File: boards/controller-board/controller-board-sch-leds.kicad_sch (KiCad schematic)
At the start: 60 parts, among them U10 MP2410A, U11 MP2410A, U6 MP2410A, U7 MP2410A, U8 MP2410A, U9 MP2410A

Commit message: Added LED test points. Added heatsinks and notes on thermal paste. Cleaned up bottom traces with new LED test points. Some hierarchical labels, some cleanup of schematic and layout. Builds.
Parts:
- added HS1, HS10, HS11, HS12, HS13, HS14, HS15, HS16, HS17, HS18, HS2, HS3, HS4, HS5, HS6, HS7, HS8, HS9: Heatsink, symbol Mechanical:Heatsink
- added TP25, TP26, TP27, TP28, TP29, TP30, TP31, TP32, TP33, TP34, TP35, TP36, TP37, TP38, TP39, TP4, TP40, TP41, TP42, TP43, TP5, TP6, TP7, TP8: TestPoint_Square, TestPoint:TestPoint_Pad_1.0x1.0mm, symbol Connector:TestPoint_Square
- C11, C13, C14, C20, C21, C22, C24, C27, C28, C30, C31, C33: DPN 1276-6767-1-ND -> 490-12456-1-ND; MFR Samsung Electro-Mechanics -> Murata Electronics; MPN CL31B106KBHNNNE -> GRT31CR61H106KE01L
- C12, C23, C25, C26, C29, C32: DPN 478-KGM15AR71H103KTCT-ND -> 399-12983-1-ND; MFR KYOCERA AVX -> KEMET; MPN KGM15AR71H103KT -> C0603C103J5RACAUTO
- R16, R17, R18, R20, R22, R6: DPN 311-1.00KHRCT-ND -> RMCF0603FT2K70CT-ND; MFR Yageo -> Stackpole Electronics; MPN RC0603FR-071KL -> RMCF0603FT1K00
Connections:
- net at C30.2, D15.1 (K), R20.2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: now also TP39.1
- net at C27.2, D12.1 (K), R18.2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: now also TP35.1
- net at C27.1, D10.2 (A), L3.2: now also TP32.1
- net at C13.2, D3.1 (K), R11.1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: now also TP7.1
- net at C22.1, D4.2 (A), L4.2: now also TP8.1
- net at C22.2, D6.1 (K), R14.1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: now also TP27.1
- net at D17.1 (K), D18.2 (A): now also TP42.1
- net at D16.1 (K), D17.2 (A): now also TP41.1
- net at D2.1 (K), D3.2 (A): now also TP6.1
- net at C33.2, D18.1 (K), R22.2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: now also TP43.1
- net at D11.1 (K), D12.2 (A): now also TP34.1
- net at D10.1 (K), D11.2 (A): now also TP33.1
- net at D14.1 (K), D15.2 (A): now also TP38.1
- net at C33.1, D16.2 (A), L7.2: now also TP40.1
- net at C21.2, D9.1 (K), R15.1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: now also TP31.1
- net at C21.1, D7.2 (A), L5.2: now also TP28.1
- net at D5.1 (K), D6.2 (A): now also TP26.1
- net at D4.1 (K), D5.2 (A): now also TP25.1
- net at D13.1 (K), D14.2 (A): now also TP37.1
- net at C30.1, D13.2 (A), L6.2: now also TP36.1
- net at C13.1, D1.2 (A), L2.2: now also TP4.1
- net at D8.1 (K), D9.2 (A): now also TP30.1
- net at D7.1 (K), D8.2 (A): now also TP29.1
- net at D1.1 (K), D2.2 (A): now also TP5.1
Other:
- note added: "(Link)"
- note added: "1206"
- note added: "ALL ON AT 100% MAY ONLY DRAW 1.5 A EACH (9 A TOTAL)"
- note added: "All resistors are 0603 1% and AEQ unless otherwise noted. All capacitors are 0603 10% X5R with Wv > 25 V and AEQ unless otherwise noted."
- note added: "Press-in HW1,HW2,HW7,and HW8 into PCB before reflowing LEDs. This will protect LED packages after reflow."
- note added: "Use thermal epoxy on heatsinks to bond to PCB. Dycotec DM-TIM-15323-SYP (DigiKey 4338-DM-TIM-15323-SYP-ND), which has 2.30 W/m-K."
- note removed: "all capacitors 50V+"
- moved on the sheet: C11, C12, C13, C14, C20, C21, C22, C23, C24, C25, C26, C27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

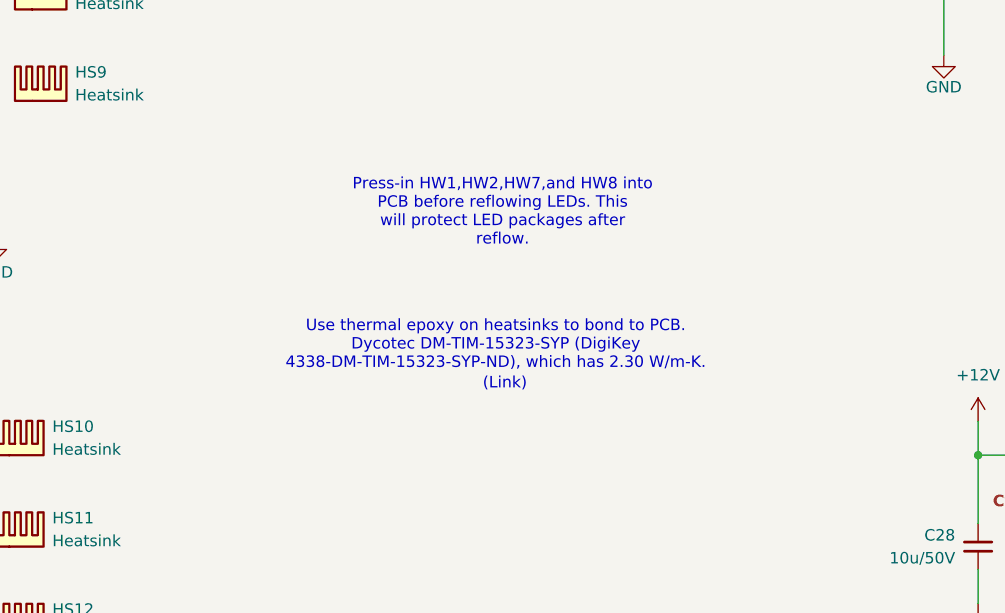
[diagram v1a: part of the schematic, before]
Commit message: Add thermal glue notes and hand-build info
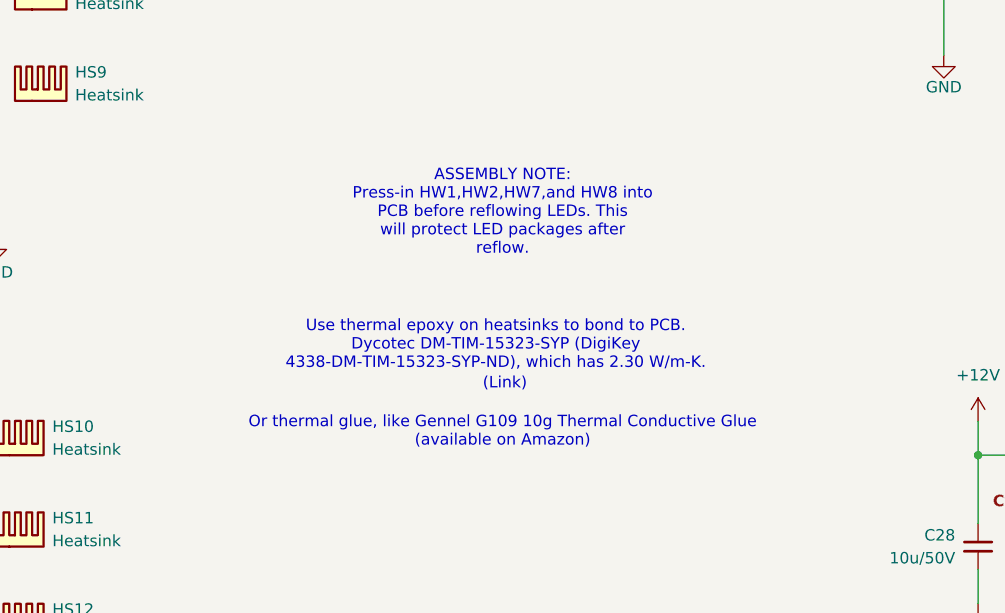
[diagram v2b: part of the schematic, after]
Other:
- note added: "ASSEMBLY NOTE: Press-in HW1,HW2,HW7,and HW8 into PCB before reflowing LEDs. This will protect LED packages after reflow."
- note added: "Or thermal glue, like Gennel G109 10g Thermal Conductive Glue (available on Amazon)"
- note removed: "Press-in HW1,HW2,HW7,and HW8 into PCB before reflowing LEDs. This will protect LED packages after reflow."
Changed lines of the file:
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@@
 		)
 	)
-	(text "Press-in HW1,HW2,HW7,and HW8 into \nPCB before reflowing LEDs. This \nwill protect LED packages after\nreflow."
+	(text "ASSEMBLY NOTE:\nPress-in HW1,HW2,HW7,and HW8 into \nPCB before reflowing LEDs. This \nwill protect LED packages after\nreflow."
 		(exclude_from_sim no)
 		(at 215.138 88.646 0)
@@
 		(effects
 			(font
+				(size 1.27 1.27)
+			)
+		)
+	)
+	(text "Or thermal glue, like Gennel G109 10g Thermal Conductive Glue\n(available on Amazon)"
+		(exclude_from_sim no)
+		(at 215.138 113.03 0)
+		(effects
+			(font
